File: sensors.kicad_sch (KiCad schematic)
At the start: 10 parts, among them U11 TCN75AVUA, U12 TCN75AVUA, U9 SC18IS604PWJ

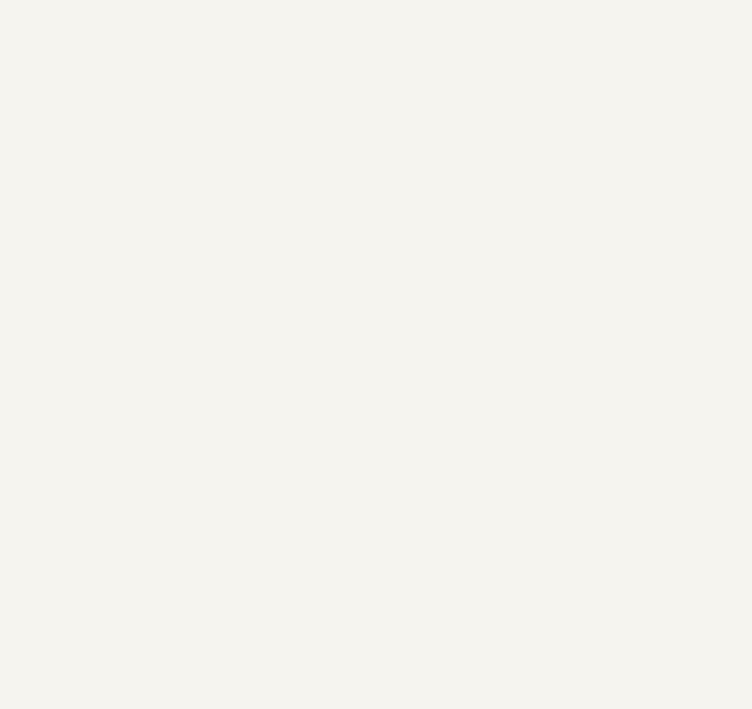
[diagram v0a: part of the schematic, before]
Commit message: Add bus debug test points
For easier debugging the I2C and SPI bus are being branched to via test
pads. Some enhancements to the PD controller are made by connecting PP5V
to ground. Also corrects the footprint of the energy meter.
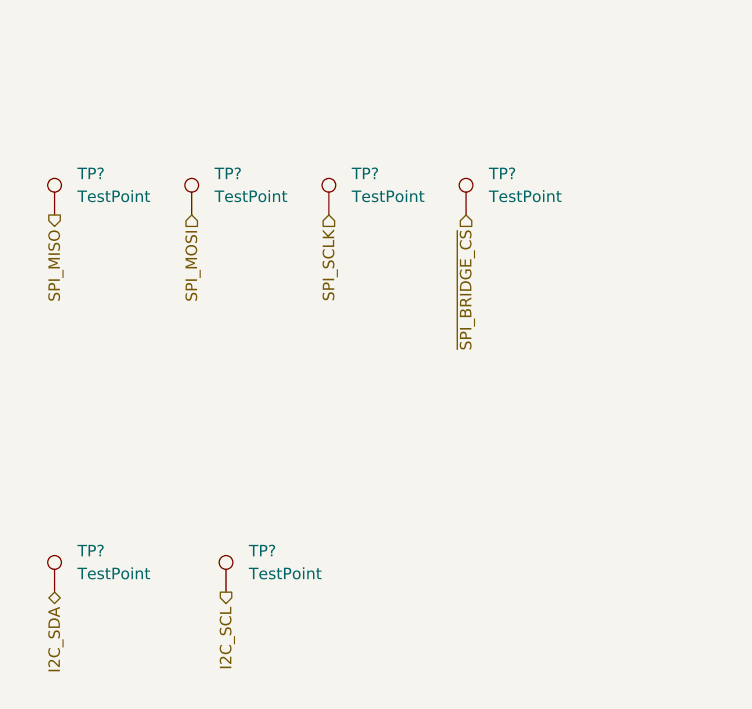
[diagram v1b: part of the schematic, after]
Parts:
- added TP? (x6): TestPoint, TestPoint:TestPoint_THTPad_D2.0mm_Drill1.0mm, symbol Connector:TestPoint
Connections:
- net I2C_SCL: now also TP?.1
- net I2C_SDA: now also TP?.1
- net SPI_MISO: now also TP?.1
- net SPI_MOSI: now also TP?.1
- net SPI_SCLK: now also TP?.1
- net ~{SPI_BRIDGE_CS}: now also TP?.1
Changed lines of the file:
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@@
+    (effects (font (size 1.27 1.27)) (justify right))
+  )
+  (hierarchical_label "SPI_SCLK" (shape input) (at 58.42 78.74 270)
     (effects (font (size 1.27 1.27)) (justify right))
   )
   (hierarchical_label "I2C_SDA" (shape bidirectional) (at 162.56 72.39 180)
+    (effects (font (size 1.27 1.27)) (justify right))
+  )
+  (hierarchical_label "I2C_SDA" (shape bidirectional) (at 27.94 120.65 270)
     (effects (font (size 1.27 1.27)) (justify right))
   )
@@
     (effects (font (size 1.27 1.27)) (justify left))
   )
+  (hierarchical_label "SPI_MISO" (shape output) (at 27.94 78.74 270)
+    (effects (font (size 1.27 1.27)) (justify right))
+  )
   (hierarchical_label "I2C_SDA" (shape bidirectional) (at 93.98 33.02 0)
     (effects (font (size 1.27 1.27)) (justify left))
@@
   )
   (hierarchical_label "I2C_SCL" (shape input) (at 161.29 34.29 180)
+    (effects (font (size 1.27 1.27)) (justify right))
+  )
+  (hierarchical_label "~{SPI_BRIDGE_CS}" (shape input) (at 73.66 78.74 270)
+    (effects (font (size 1.27 1.27)) (justify right))
+  )
+  (hierarchical_label "SPI_MOSI" (shape input) (at 43.18 78.74 270)
+    (effects (font (size 1.27 1.27)) (justify right))
+  )
+  (hierarchical_label "I2C_SCL" (shape output) (at 46.99 120.65 270)
     (effects (font (size 1.27 1.27)) (justify right))
   )
@@
     (pin "1")
   )
+  (symbol (lib_id "Connector:TestPoint") (at 46.99 120.65 0) (unit 1)
+    (in_bom yes) (on_board yes) (fields_autoplaced)
+    (property "Reference" "TP?" (id 0) (at 49.53 116.0779 0)
+      (effects (font (size 1.27 1.27)) (justify left))
+    )
+    (property "Value" "TestPoint" (id 1) (at 49.53 118.6179 0)
+      (effects (font (size 1.27 1.27)) (justify left))
+    )
+    (property "Footprint" "TestPoint:TestPoint_THTPad_D2.0mm_Drill1.0mm" (id 2) (at 52.07 120.65 0)
+      (effects (font (size 1.27 1.27)) hide)
+    )
+    (property "Datasheet" "~" (id 3) (at 52.07 120.65 0)
+      (effects (font (size 1.27 1.27)) hide)
+    )
+    (pin "1")
+  )
   (symbol (lib_id "power:+3.3V") (at 34.29 35.56 0) (unit 1)
     (in_bom yes) (on_board yes) (fields_autoplaced)
@@
     (pin "1")
   )
+  (symbol (lib_id "Connector:TestPoint") (at 27.94 78.74 0) (unit 1)
+    (in_bom yes) (on_board yes) (fields_autoplaced)
+    (property "Reference" "TP?" (id 0) (at 30.48 74.1679 0)
+      (effects (font (size 1.27 1.27)) (justify left))
+    )
+    (property "Value" "TestPoint" (id 1) (at 30.48 76.7079 0)
+      (effects (font (size 1.27 1.27)) (justify left))
+    )
+    (property "Footprint" "TestPoint:TestPoint_THTPad_D2.0mm_Drill1.0mm" (id 2) (at 33.02 78.74 0)
+      (effects (font (size 1.27 1.27)) hide)
+    )
+    (property "Datasheet" "~" (id 3) (at 33.02 78.74 0)
+      (effects (font (size 1.27 1.27)) hide)
+    )
+    (pin "1")
+  )
   (symbol (lib_id "power:GND") (at 189.23 39.37 0) (unit 1)
     (in_bom yes) (on_board yes) (fields_autoplaced)
@@
     )
     (property "Datasheet" "" (id 3) (at 209.55 80.01 0)
+      (effects (font (size 1.27 1.27)) hide)
+    )
+    (pin "1")
+  )
+  (symbol (lib_id "Connector:TestPoint") (at 73.66 78.74 0) (unit 1)
+    (in_bom yes) (on_board yes) (fields_autoplaced)
+    (property "Reference" "TP?" (id 0) (at 76.2 74.1679 0)
+      (effects (font (size 1.27 1.27)) (justify left))
+    )
+    (property "Value" "TestPoint" (id 1) (at 76.2 76.7079 0)
+      (effects (font (size 1.27 1.27)) (justify left))
+    )
+    (property "Footprint" "TestPoint:TestPoint_THTPad_D2.0mm_Drill1.0mm" (id 2) (at 78.74 78.74 0)
+      (effects (font (size 1.27 1.27)) hide)
+    )
+    (property "Datasheet" "~" (id 3) (at 78.74 78.74 0)
       (effects (font (size 1.27 1.27)) hide)
     )
@@
     (pin "9")
   )
+  (symbol (lib_id "Connector:TestPoint") (at 43.18 78.74 0) (unit 1)
+    (in_bom yes) (on_board yes) (fields_autoplaced)
+    (property "Reference" "TP?" (id 0) (at 45.72 74.1679 0)
+      (effects (font (size 1.27 1.27)) (justify left))
+    )
+    (property "Value" "TestPoint" (id 1) (at 45.72 76.7079 0)
+      (effects (font (size 1.27 1.27)) (justify left))
+    )
+    (property "Footprint" "TestPoint:TestPoint_THTPad_D2.0mm_Drill1.0mm" (id 2) (at 48.26 78.74 0)
+      (effects (font (size 1.27 1.27)) hide)
+    )
+    (property "Datasheet" "~" (id 3) (at 48.26 78.74 0)
+      (effects (font (size 1.27 1.27)) hide)
+    )
+    (pin "1")
+  )
+  (symbol (lib_id "Connector:TestPoint") (at 27.94 120.65 0) (unit 1)
+    (in_bom yes) (on_board yes) (fields_autoplaced)
+    (property "Reference" "TP?" (id 0) (at 30.48 116.0779 0)
+      (effects (font (size 1.27 1.27)) (justify left))
+    )
+    (property "Value" "TestPoint" (id 1) (at 30.48 118.6179 0)
+      (effects (font (size 1.27 1.27)) (justify left))
+    )
+    (property "Footprint" "TestPoint:TestPoint_THTPad_D2.0mm_Drill1.0mm" (id 2) (at 33.02 120.65 0)
+      (effects (font (size 1.27 1.27)) hide)
+    )
+    (property "Datasheet" "~" (id 3) (at 33.02 120.65 0)
+      (effects (font (size 1.27 1.27)) hide)
+    )
+    (pin "1")
+  )
   (symbol (lib_id "power:+3.3V") (at 209.55 72.39 0) (unit 1)
     (in_bom yes) (on_board yes) (fields_autoplaced)
@@
       (effects (font (size 1.27 1.27)) hide)
     )
+    (pin "1")
+  )
+  (symbol (lib_id "Connector:TestPoint") (at 58.42 78.74 0) (unit 1)
+    (in_bom yes) (on_board yes) (fields_autoplaced)
+    (property "Reference" "TP?" (id 0) (at 60.96 74.1679 0)
+      (effects (font (size 1.27 1.27)) (justify left))
+    )
+    (property "Value" "TestPoint" (id 1) (at 60.96 76.7079 0)
+      (effects (font (size 1.27 1.27)) (justify left))
+    )
+    (property "Footprint" "TestPoint:TestPoint_THTPad_D2.0mm_Drill1.0mm" (id 2) (at 63.5 78.74 0)
+      (effects (font (size 1.27 1.27)) hide)
+    )
+    (property "Datasheet" "~" (id 3) (at 63.5 78.74 0)
+      (effects (font (size 1.27 1.27)) hide)
+    )

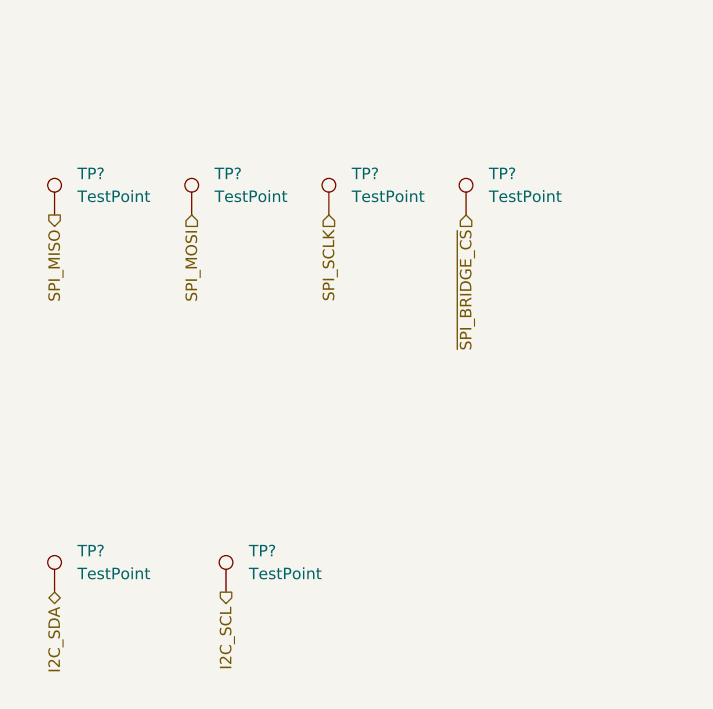
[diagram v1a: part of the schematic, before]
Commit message: Update readme, add PD controller config
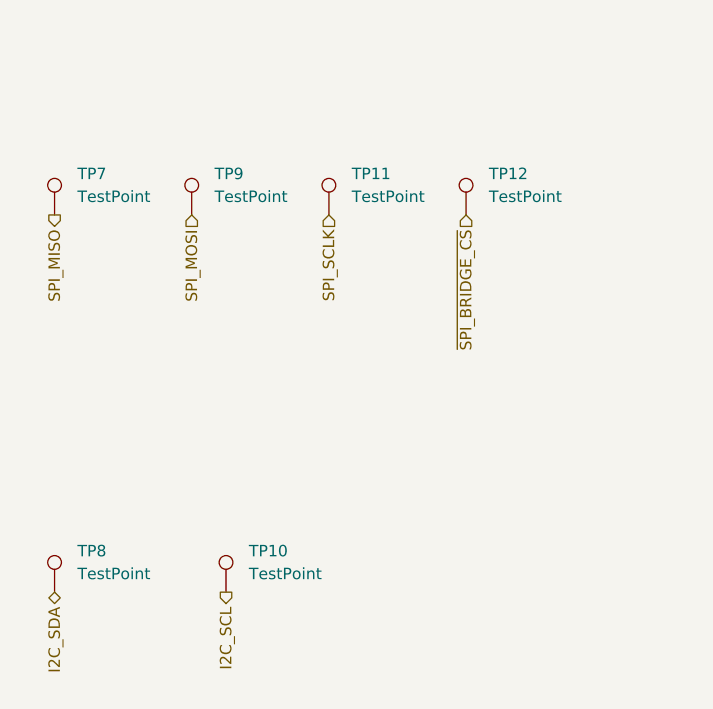
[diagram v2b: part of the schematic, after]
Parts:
- gave numbers to parts that had none: 6
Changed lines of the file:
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@@
   (symbol (lib_id "Connector:TestPoint") (at 46.99 120.65 0) (unit 1)
     (in_bom yes) (on_board yes) (fields_autoplaced)
-    (property "Reference" "TP?" (id 0) (at 49.53 116.0779 0)
+    (property "Reference" "TP10" (id 0) (at 49.53 116.0779 0)
       (effects (font (size 1.27 1.27)) (justify left))
     )
@@
   (symbol (lib_id "Connector:TestPoint") (at 27.94 78.74 0) (unit 1)
     (in_bom yes) (on_board yes) (fields_autoplaced)
-    (property "Reference" "TP?" (id 0) (at 30.48 74.1679 0)
+    (property "Reference" "TP7" (id 0) (at 30.48 74.1679 0)
       (effects (font (size 1.27 1.27)) (justify left))
     )
@@
   (symbol (lib_id "Connector:TestPoint") (at 73.66 78.74 0) (unit 1)
     (in_bom yes) (on_board yes) (fields_autoplaced)
-    (property "Reference" "TP?" (id 0) (at 76.2 74.1679 0)
+    (property "Reference" "TP12" (id 0) (at 76.2 74.1679 0)
       (effects (font (size 1.27 1.27)) (justify left))
     )
@@
   (symbol (lib_id "Connector:TestPoint") (at 43.18 78.74 0) (unit 1)
     (in_bom yes) (on_board yes) (fields_autoplaced)
-    (property "Reference" "TP?" (id 0) (at 45.72 74.1679 0)
+    (property "Reference" "TP9" (id 0) (at 45.72 74.1679 0)
       (effects (font (size 1.27 1.27)) (justify left))
     )
@@
   (symbol (lib_id "Connector:TestPoint") (at 27.94 120.65 0) (unit 1)
     (in_bom yes) (on_board yes) (fields_autoplaced)
-    (property "Reference" "TP?" (id 0) (at 30.48 116.0779 0)
+    (property "Reference" "TP8" (id 0) (at 30.48 116.0779 0)
       (effects (font (size 1.27 1.27)) (justify left))
     )
@@
   (symbol (lib_id "Connector:TestPoint") (at 58.42 78.74 0) (unit 1)
     (in_bom yes) (on_board yes) (fields_autoplaced)
-    (property "Reference" "TP?" (id 0) (at 60.96 74.1679 0)
-      (effects (font (size 1.27 1.27)) (justify left))
-    )
+    (property "Reference" "TP11" (id 0) (at 60.96 74.1679 0)
+      (effects (font (size 1.27 1.27)) (justify left))
+    )
